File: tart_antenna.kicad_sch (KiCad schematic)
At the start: 10 parts, among them J1 RFShield_OnePiece, J2 Conn_Coaxial, U1 5400BL15B050, U2 BGU7005

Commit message: Added sheet template
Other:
- company: (none) -> The Transient Array Radio Telescope
- title: (none) -> TART Active Antenna
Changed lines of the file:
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@@
 (kicad_sch (version 20211123) (generator eeschema)
   (paper "A4")
+  (title_block
+    (title "TART Active Antenna")
+    (date "2022-09-15")
+    (rev "0.1")
+    (company "The Transient Array Radio Telescope")
+    (comment 1 "Tim Molteno (tim@elec.ac.nz)")
+  )
   (junction (at 185.42 93.98) (diameter 0) (color 0 0 0 0)
   )

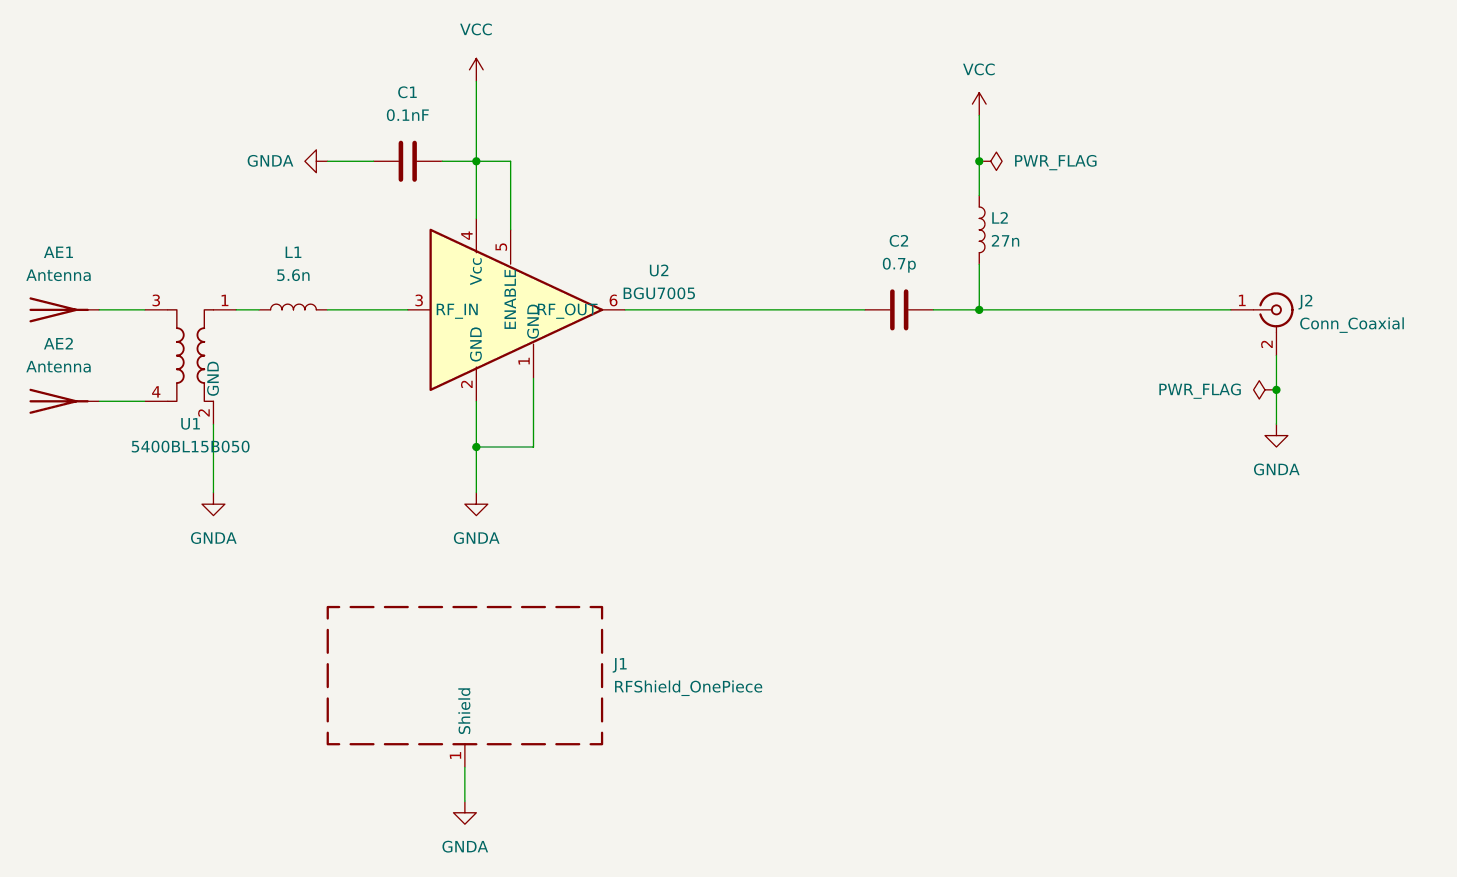
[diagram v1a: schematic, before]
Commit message: Added round background
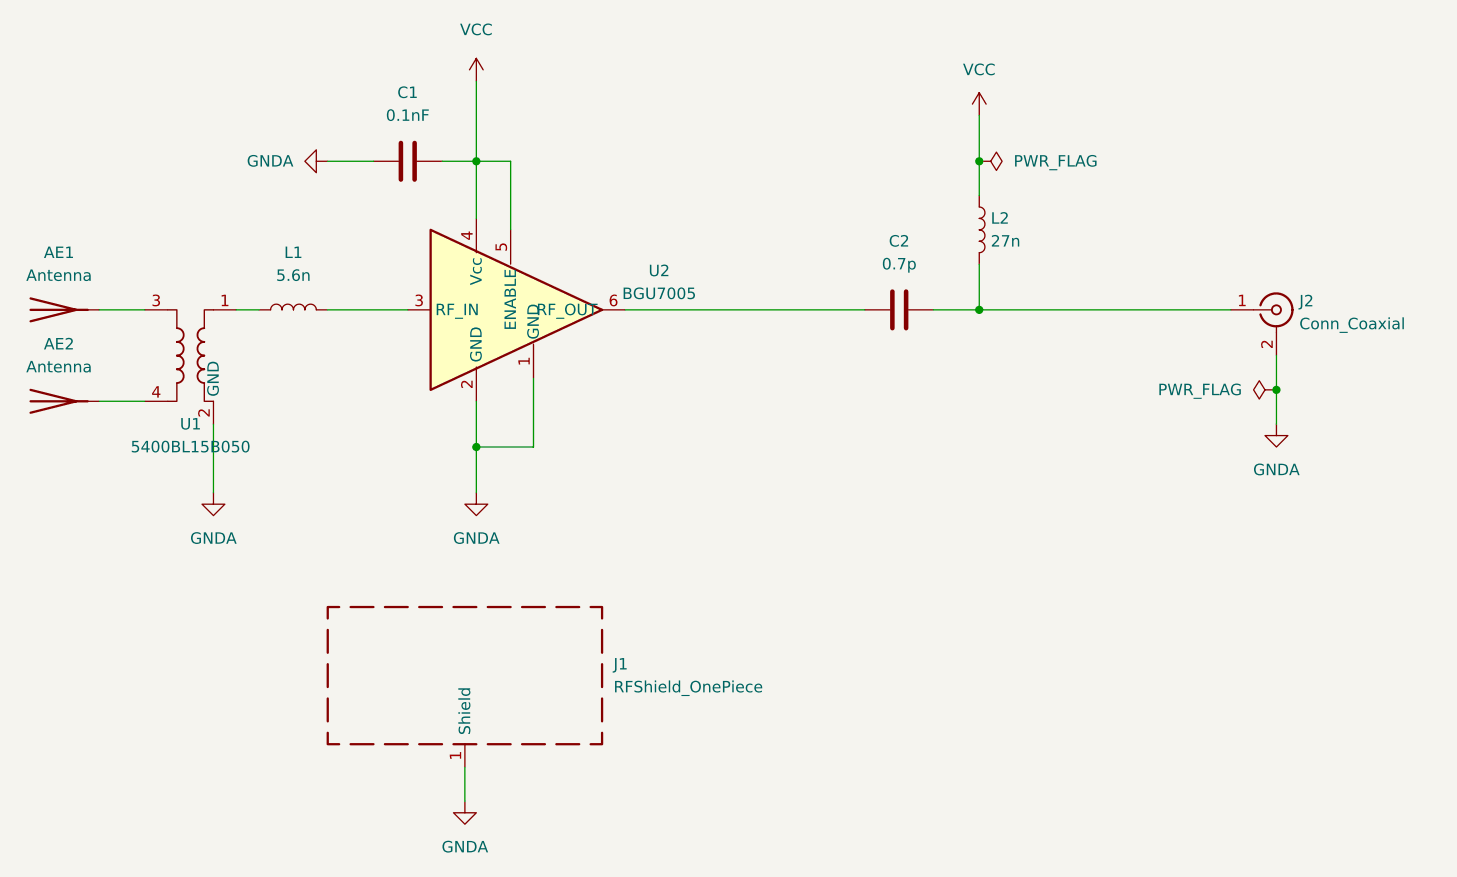
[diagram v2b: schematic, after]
